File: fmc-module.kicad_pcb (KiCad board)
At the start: 4 copper layers, 85 x 71 mm, 64 parts, among them J2 501951-2230, J4 Conn_01x02, J5 HDMI_A, J6 Conn_01x03, SW1 SW_DIP_x03, U1 TFP410PAPR, U2 MIC5205-5.0YM5, U6 W956D8NBRA5I, U8 PCA9306DCU

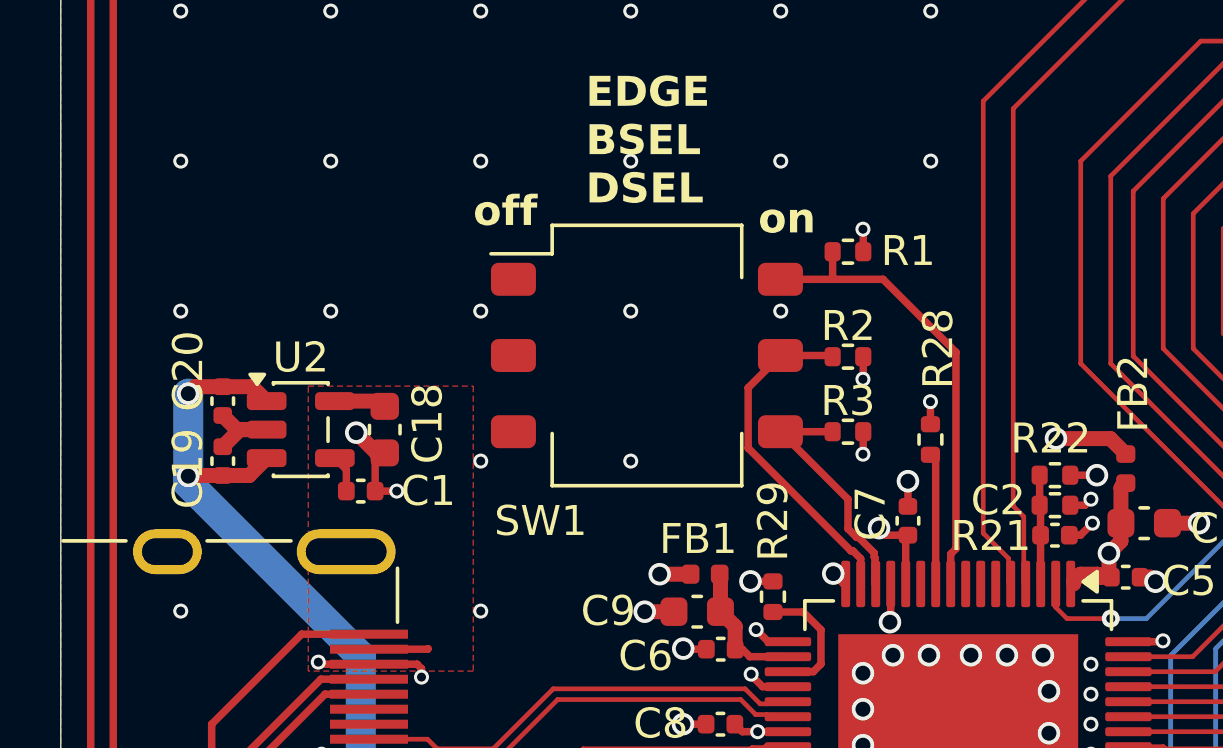
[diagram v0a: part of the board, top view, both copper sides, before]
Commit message: Fixed wrong FMC pin labels
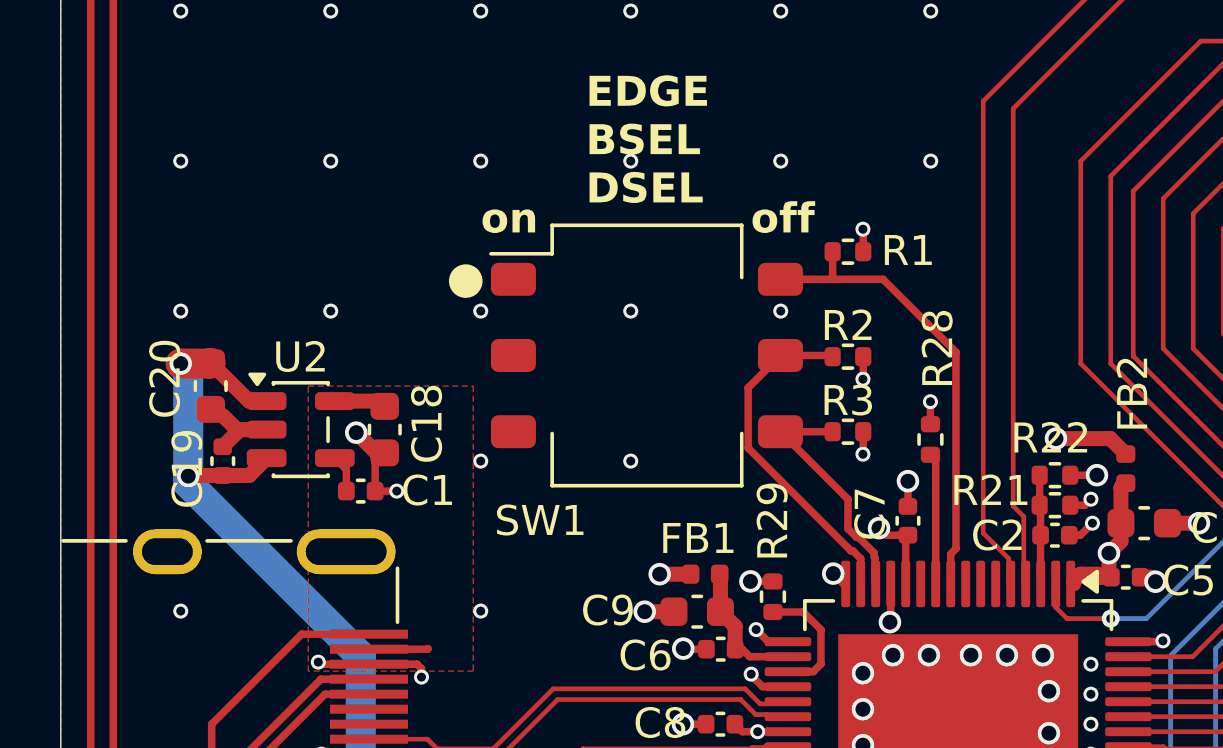
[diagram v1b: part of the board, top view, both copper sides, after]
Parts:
- C20: value 0.1uF -> 10uF; footprint Capacitor_SMD:C_0402_1005Metric -> Capacitor_SMD:C_0603_1608Metric
- moved C20 0.64 mm to (91.0, 107.5)
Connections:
- net /fmc/fmc_LA17_N renamed /fmc/fmc_LA17_P
- J1 pad D26: /fmc/fmc_LA26_N -> /fmc/fmc_LA26_P
- J1 pad D27: /fmc/fmc_LA26_P -> /fmc/fmc_LA26_N
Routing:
- net +12V: track 159.5 -> 161.1 mm
